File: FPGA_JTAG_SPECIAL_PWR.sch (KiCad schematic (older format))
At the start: 18 parts, among them U900 GW1N-9LQ100

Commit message: Stuff
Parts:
- added C36, C37, C38, C39, C56, C57, C58, C59, C60: 100nF_0603_Ceramic_Capacitor,_10%,_X7R,_25V, symbol OpenVent:100nF_0603_Ceramic_Capacitor,_10%,_X7R,_25V
- added C62, C63: 1uF_0603_Ceramic_Capacitor,_10%,_50V,_X5R, Capacitor_SMD:C_0603_1608Metric, symbol OpenVent:1uF_0603_Ceramic_Capacitor,_10%,_50V,_X5R
- added C65, C66: 10uF_0805_Ceramic_Capacitor_10%_X7R_10V, Capacitor_SMD:C_0805_2012Metric, symbol OpenVent:10uF_0805_Ceramic_Capacitor_10%_X7R_10V
- gave numbers to parts that had none: 13
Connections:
- wire segments 84 -> 139
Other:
- note added: "200 Ohm Res on the reset to GND"
- note added: "Fix arrow direction\n\n"
- note added: "HAS TO BE LDO"
- note added: "Same value caps. Occaisional big one."
- note added: "change to 0.1uF\n"

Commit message: First cut at a 3D rendering of the board.  Not too many missing models...
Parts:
- added R?: R_0603_200_0.1W_1%, Resistor_SMD:R_0603_1608Metric, symbol OpenVent:R_0603_200_0.1W_1%
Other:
- moved on the sheet: C24, C36, C37, C38, C39, C56, C57, C58, C59, C60, C62, C63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

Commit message: Changes some stuff
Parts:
- removed C24: 10uF_0805_Ceramic_Capacitor_10%_X7R_10V, Capacitor_SMD:C_0805_2012Metric, symbol OpenVent:10uF_0805_Ceramic_Capacitor_10%_X7R_10V
- removed C62, C63: 1uF_0603_Ceramic_Capacitor,_10%,_50V,_X5R, Capacitor_SMD:C_0603_1608Metric, symbol OpenVent:1uF_0603_Ceramic_Capacitor,_10%,_50V,_X5R
- added C21, C24, C61, C62: 100nF_0603_Ceramic_Capacitor,_10%,_X7R,_25V, symbol OpenVent:100nF_0603_Ceramic_Capacitor,_10%,_X7R,_25V
- added C63: 10uF_0805_Ceramic_Capacitor_10%_X7R_10V, Capacitor_SMD:C_0805_2012Metric, symbol OpenVent:10uF_0805_Ceramic_Capacitor_10%_X7R_10V
- gave numbers to parts that had none: 1
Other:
- note removed: "200 Ohm Res on the reset to GND"
- note removed: "Same value caps. Occaisional big one."
- note removed: "change to 0.1uF\n"
- moved on the sheet: C66

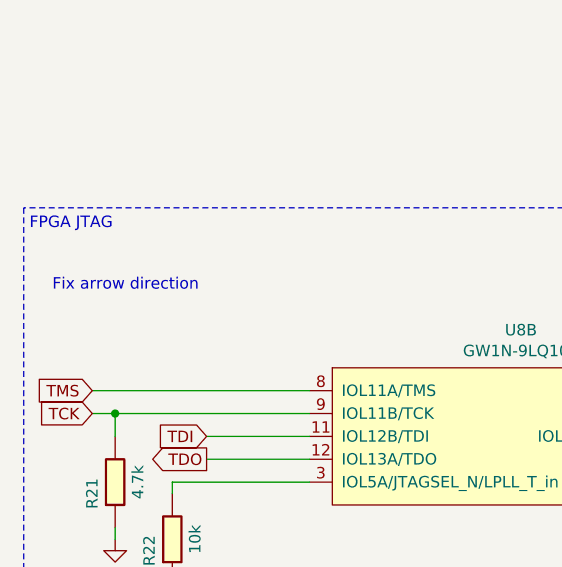
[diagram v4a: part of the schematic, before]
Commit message: Went through the whole circuit and made a note of what needs changing
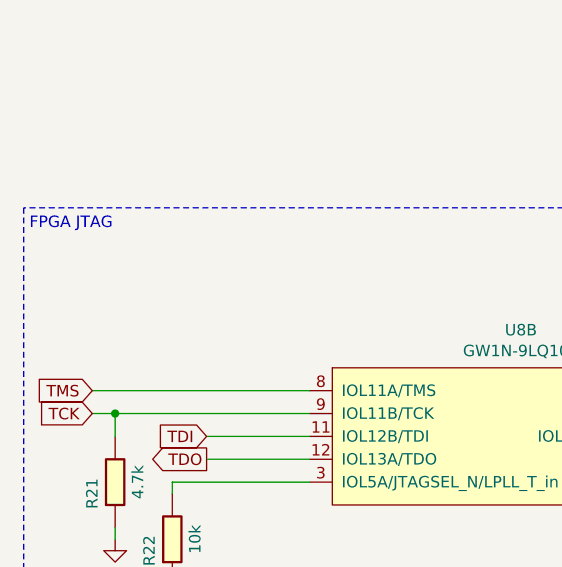
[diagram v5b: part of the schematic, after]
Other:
- note removed: "Fix arrow direction\n\n"
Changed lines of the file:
@@
 Text Notes 6875 1025 0    50   ~ 0
 HAS TO BE LDO
-Text Notes 1025 4850 0    50   ~ 0
-Fix arrow direction\n\n
 $Comp
 L OpenVent:12k_0603_Chip_Resistor,_1%,_0.1W R?

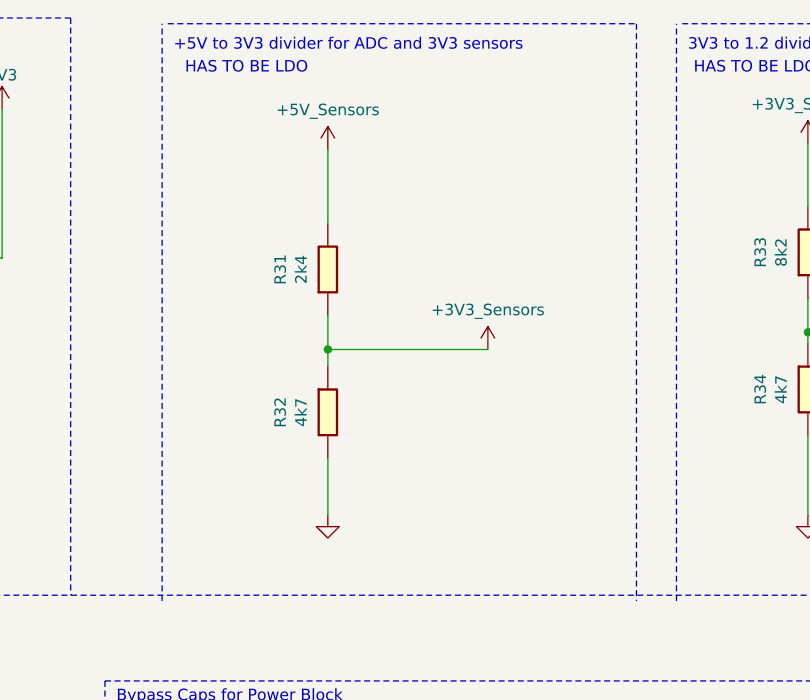
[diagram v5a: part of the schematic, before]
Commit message: Detailed description of changes below:
Sheet 2:
WD protection: 33ohm resistor in series in each line and then on the side between the resistor and micro put the ESD diode
ferrite beads and ESD prot on JP2
NRST PULLED UP TO 3V3Always on
VDD USB to 3V3
Sheet 6:
Oscillator out put to pin 40, got rud of 15pf
pin one pull up to 3v3 by 10k
Sheet 7:
changed 3V3 sensors from divider to LDO
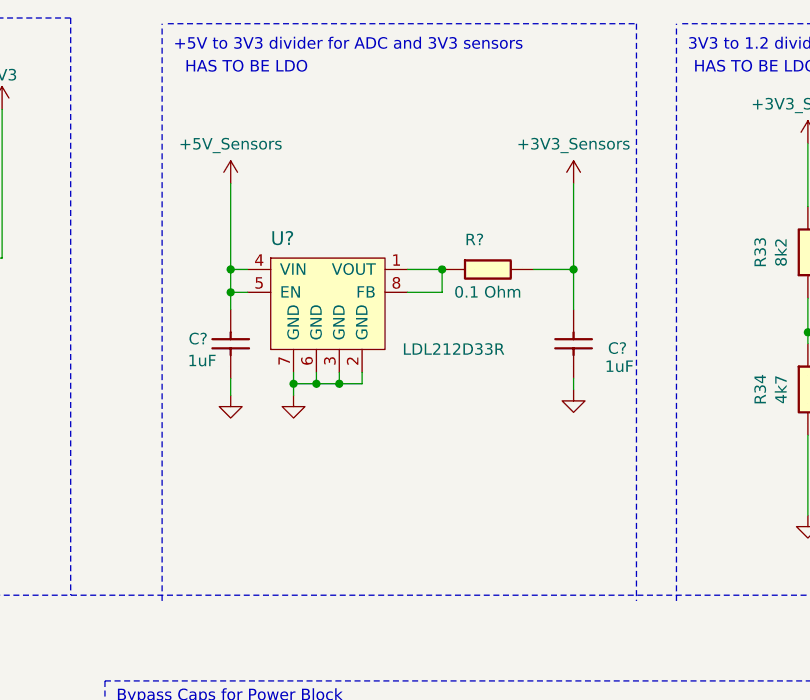
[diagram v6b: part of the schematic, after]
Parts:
- removed R31: 2k4_0603_Chip_Resistor,_1%,_0.1W, Resistor_SMD:R_0603_1608Metric, symbol OpenVent:2k4_0603_Chip_Resistor,_1%,_0.1W
- removed R32: 4k7_0603_Chip_Resistor,_1%,_0.1W, symbol OpenVent:4k7_0603_Chip_Resistor,_1%,_0.1W
- added C? (x2): 1uF_0603_Ceramic_Capacitor,_10%,_50V,_X5R, Capacitor_SMD:C_0603_1608Metric, symbol OpenVent:1uF_0603_Ceramic_Capacitor,_10%,_50V,_X5R
- added R?: 0R1_0603_Chip_Resistor,_1%,_0.1W, Resistor_SMD:R_0603_1608Metric, symbol OpenVent:0R1_0603_Chip_Resistor,_1%,_0.1W
- added U?: LDL212D33R, Package_SO:SO-8_5.3x6.2mm_P1.27mm, symbol OpenVent:LDL212D33R
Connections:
- net +3.3V: now also C?.1, R?.2
- net +5V: now also C?.2, U?.4 (VIN), U?.5 (EN)
- net GND: now also C?.1, C?.2, U?.2 (GND), U?.3 (GND), U?.6 (GND), U?.7 (GND)
- new net: R?.1, U?.1 (VOUT), U?.8 (FB)
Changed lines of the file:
@@
 	3625 1550 3625 1675
-$Comp
-L OpenVent:4k7_0603_Chip_Resistor,_1%,_0.1W R32
-U 1 1 5FCAA592
-P 7600 2400
-F 0 "R32" H 7500 2707 50  0000 C CNN
-F 1 "4k7_0603_Chip_Resistor,_1%,_0.1W" H 7600 2400 50  0001 C CNN
-F 2 "" H 7600 2400 50  0001 C CNN
-F 3 "" H 7600 2400 60  0001 C CNN
-F 4 "4k7" H 7500 2616 50  0000 C CNN "Val"
-F 5 "1%" H 7600 2400 50  0001 C CNN "Tolerance"
-F 6 "0.1W" H 7600 2400 50  0001 C CNN "Watt"
-	1    7600 2400
-	0    -1   -1   0
-$EndComp
-$Comp
-L OpenVent:2k4_0603_Chip_Resistor,_1%,_0.1W R31
-U 1 1 5FCB7193
-P 7400 1975
-F 0 "R31" H 7500 2082 50  0000 C CNN
-F 1 "2k4_0603_Chip_Resistor,_1%,_0.1W" H 7400 1975 50  0001 C CNN
-F 2 "Resistor_SMD:R_0603_1608Metric" H 7400 1975 50  0001 C CNN
-F 3 "" H 7400 1975 50  0001 C CNN
-F 4 "2k4" H 7500 1991 50  0000 C CNN "Val"
-F 5 "1%" H 7400 1975 50  0001 C CNN "Tolerance"
-F 6 "0.1W" H 7400 1975 50  0001 C CNN "Watt"
-	1    7400 1975
-	0    -1   -1   0
-$EndComp
 $Comp
 L OpenVent:8k2_0603_Chip_Resistor,_1%,_0.1W R33
@@
 	0    -1   -1   0
 $EndComp
-Wire Wire Line
-	7500 2300 7500 2225
 $Comp
 L OpenVent:GND #PWR?
 U 1 1 5FCCFD82
-P 7500 2950
+P 7075 2425
 AR Path="/5F8F8987/5FCCFD82" Ref="#PWR?"  Part="1"
 AR Path="/5FB692C4/5FCCFD82" Ref="#PWR064"  Part="1"
 AR Path="/5FBE8499/5FCCFD82" Ref="#PWR068"  Part="1"
-F 0 "#PWR068" H 7500 2700 50  0001 C CNN
-F 1 "GND" H 7500 2800 50  0001 C CNN
-F 2 "" H 7500 2950 50  0001 C CNN
-F 3 "" H 7500 2950 50  0001 C CNN
-	1    7500 2950
-	1    0    0    -1
-$EndComp
-Wire Wire Line
-	7500 2700 7500 2950
-Wire Wire Line
-	7500 2225 8200 2225
-Connection ~ 7500 2225
-Wire Wire Line
-	7500 2225 7500 2075
-Wire Wire Line
-	7500 1350 7500 1675
+F 0 "#PWR068" H 7075 2175 50  0001 C CNN
+F 1 "GND" H 7075 2275 50  0001 C CNN
+F 2 "" H 7075 2425 50  0001 C CNN
+F 3 "" H 7075 2425 50  0001 C CNN
+	1    7075 2425
+	1    0    0    -1
+$EndComp
 $Comp
 L OpenVent:GND #PWR?
@@
 L OpenVent:+5V_Sensors #PWR067
 U 1 1 5FBC8B4F
-P 7500 1350
-F 0 "#PWR067" H 7500 1200 50  0001 C CNN
-F 1 "+5V_Sensors" H 7500 1523 50  0000 C CNN
-F 2 "" H 7500 1350 50  0001 C CNN
-F 3 "" H 7500 1350 50  0001 C CNN
-	1    7500 1350
+P 7075 1500
+F 0 "#PWR067" H 7075 1350 50  0001 C CNN
+F 1 "+5V_Sensors" H 7075 1673 50  0000 C CNN
+F 2 "" H 7075 1500 50  0001 C CNN
+F 3 "" H 7075 1500 50  0001 C CNN
+	1    7075 1500
 	1    0    0    -1
 $EndComp
@@
 Text Notes 5475 1600 1    50   ~ 0
 DO NOT FIT
-Wire Wire Line
-	5175 1825 6075 1825
 Wire Wire Line
 	2325 1800 2325 2325
@@
 L OpenVent:+3V3_Sensors #PWR?
 U 1 1 5FC9D143
-P 8200 2225
+P 8575 1500
 AR Path="/5FC9D143" Ref="#PWR?"  Part="1"
 AR Path="/5FB692C4/5FC9D143" Ref="#PWR?"  Part="1"
 AR Path="/5FBE8499/5FC9D143" Ref="#PWR069"  Part="1"
-F 0 "#PWR069" H 8200 2075 50  0001 C CNN
-F 1 "+3V3_Sensors" H 8200 2398 50  0000 C CNN
-F 2 "" H 8200 2225 50  0001 C CNN
-F 3 "" H 8200 2225 50  0001 C CNN
-	1    8200 2225
+F 0 "#PWR069" H 8575 1350 50  0001 C CNN
+F 1 "+3V3_Sensors" H 8575 1673 50  0000 C CNN
+F 2 "" H 8575 1500 50  0001 C CNN
+F 3 "" H 8575 1500 50  0001 C CNN
+	1    8575 1500
 	1    0    0    -1
 $EndComp
@@
 Wire Wire Line
 	9525 5325 10150 5325
+$Comp
+L OpenVent:GND #PWR?
+U 1 1 5FEC0980
+P 7350 2425
+AR Path="/5F99D63D/5FEC0980" Ref="#PWR?"  Part="1"
+AR Path="/5FBE8499/5FEC0980" Ref="#PWR?"  Part="1"
+F 0 "#PWR?" H 7350 2425 50  0001 C CNN
+F 1 "GND" H 7350 2425 50  0001 C CNN
+F 2 "" H 7350 2425 50  0001 C CNN
+F 3 "" H 7350 2425 50  0001 C CNN
+	1    7350 2425
+	1    0    0    -1
+$EndComp
+$Comp
+L OpenVent:LDL212D33R U?
+U 1 1 5FEC0997
+P 7500 2025
+AR Path="/5F99D63D/5FEC0997" Ref="U?"  Part="1"
+AR Path="/5FBE8499/5FEC0997" Ref="U?"  Part="1"
+F 0 "U?" H 7250 2275 60  0000 L BNN
+F 1 "LDL212D33R" H 8050 1825 50  0000 C CNN
+F 2 "Package_SO:SO-8_5.3x6.2mm_P1.27mm" H 7500 2025 50  0001 C CNN
+F 3 "https://www.st.com/resource/en/datasheet/ldl212.pdf" H 7500 2025 50  0001 C CNN
+F 4 "LDL212D33R" H 7500 2025 50  0001 C CNN "Mfr_PN"
+F 5 "STMicroelectronics" H 7500 2025 50  0001 C CNN "Mfr"
+F 6 "1.2A" H 7500 2025 50  0001 C CNN "Current"
+F 7 "LDOVOLTAGE REGULATORS 1.2A LOW D" H 7500 2025 50  0001 C CNN "Desc"
+F 8 "Linear Voltage Regulator IC Output 1.2A 8-SO" H 7500 2025 50  0001 C CNN "Detailed"
+F 9 "DigiKey" H 7500 2025 50  0001 C CNN "DistName"
+F 10 "497-18287-2-ND" H 7500 2025 50  0001 C CNN "Dist_PN"
+	1    7500 2025
+	1    0    0    -1
+$EndComp
+$Comp
+L OpenVent:1uF_0603_Ceramic_Capacitor,_10%,_50V,_X5R C?
+U 1 1 5FEC09A0
+P 8675 2150
+AR Path="/5F99D63D/5FEC09A0" Ref="C?"  Part="1"
+AR Path="/5FBE8499/5FEC09A0" Ref="C?"  Part="1"
+F 0 "C?" V 8775 2200 50  0000 L BNN
+F 1 "1uF_0603_Ceramic_Capacitor,_10%,_50V,_X5R" V 8585 1960 50  0001 C CNN
+F 2 "Capacitor_SMD:C_0603_1608Metric" H 8585 1960 50  0001 C CNN
+F 3 "" H 8585 1960 50  0001 C CNN
+F 4 "10%" H 8675 2150 50  0001 C CNN "Tolerance"
+F 5 "1uF" V 8825 2250 50  0000 C CNN "Val"
+F 6 "50V" H 8675 2150 50  0001 C CNN "Voltage"
+	1    8675 2150
+	0    1    1    0
+$EndComp
+$Comp
+L OpenVent:0R1_0603_Chip_Resistor,_1%,_0.1W R?
+U 1 1 5FEC09A9
+P 8100 1775
+AR Path="/5FEC09A9" Ref="R?"  Part="1"
+AR Path="/5F99D63D/5FEC09A9" Ref="R?"  Part="1"
+AR Path="/5FBE8499/5FEC09A9" Ref="R?"  Part="1"
+F 0 "R?" H 8100 1775 50  0000 L BNN
+F 1 "0R1_0603_Chip_Resistor,_1%,_0.1W" H 8100 1525 50  0001 C CNN
+F 2 "Resistor_SMD:R_0603_1608Metric" H 8100 1435 50  0001 C CNN
+F 3 "" H 8100 1435 50  0001 C CNN
+F 4 "1%" V -300 -4525 50  0001 C CNN "Tolerance"
+F 5 "0.1 Ohm" H 8200 1575 50  0000 C CNN "Val"
+F 6 "0.1W" H 8100 1775 50  0001 C CNN "Watt"
+	1    8100 1775
+	1    0    0    -1
+$EndComp
+$Comp
+L OpenVent:1uF_0603_Ceramic_Capacitor,_10%,_50V,_X5R C?
+U 1 1 5FEC09B2
+P 6975 2250
+AR Path="/5F99D63D/5FEC09B2" Ref="C?"  Part="1"
+AR Path="/5FBE8499/5FEC09B2" Ref="C?"  Part="1"
+F 0 "C?" V 7075 2250 50  0000 L BNN
+F 1 "1uF_0603_Ceramic_Capacitor,_10%,_50V,_X5R" V 6885 2060 50  0001 C CNN
+F 2 "Capacitor_SMD:C_0603_1608Metric" H 6885 2060 50  0001 C CNN
+F 3 "" H 6885 2060 50  0001 C CNN
+F 4 "10%" H 6975 2250 50  0001 C CNN "Tolerance"
+F 5 "1uF" V 6950 2275 50  0000 C CNN "Val"
+F 6 "50V" H 6975 2250 50  0001 C CNN "Voltage"
+	1    6975 2250
+	0    -1   -1   0
+$EndComp
+Wire Wire Line
+	7850 1875 8000 1875
+Wire Wire Line
+	7850 1975 8000 1975
+Wire Wire Line
+	8000 1975 8000 1875
+Wire Wire Line
+	7350 2325 7350 2375
+Wire Wire Line
+	7350 2375 7450 2375
+Wire Wire Line
+	7650 2375 7650 2325
+Connection ~ 7350 2375
+Wire Wire Line
+	7350 2375 7350 2425
+Wire Wire Line
+	7550 2325 7550 2375
+Connection ~ 7550 2375
+Wire Wire Line
+	7550 2375 7650 2375
+Wire Wire Line
+	7450 2325 7450 2375
+Connection ~ 7450 2375
+Wire Wire Line
+	7450 2375 7550 2375
+Wire Wire Line
+	5175 1825 6075 1825
+Wire Wire Line
+	7075 1500 7075 1875
+Connection ~ 7075 1875
+Wire Wire Line
+	7075 1875 7150 1875
+Wire Wire Line
+	7075 1875 7075 1975
+Wire Wire Line
+	7075 1975 7150 1975
+Wire Wire Line
+	7075 2425 7075 2350
+Wire Wire Line
+	7075 2050 7075 1975
+Connection ~ 7075 1975
+Connection ~ 8000 1875
+Wire Wire Line
+	8575 1500 8575 1875
+Wire Wire Line
+	8400 1875 8575 1875
+Connection ~ 8575 1875
+Wire Wire Line
+	8575 1875 8575 2050
+$Comp
+L OpenVent:GND #PWR?
+U 1 1 5FF69BE4
+P 8575 2400
+AR Path="/5F99D63D/5FF69BE4" Ref="#PWR?"  Part="1"
+AR Path="/5FBE8499/5FF69BE4" Ref="#PWR?"  Part="1"
+F 0 "#PWR?" H 8575 2400 50  0001 C CNN
+F 1 "GND" H 8575 2400 50  0001 C CNN
+F 2 "" H 8575 2400 50  0001 C CNN
+F 3 "" H 8575 2400 50  0001 C CNN
+	1    8575 2400
+	1    0    0    -1
+$EndComp
+Wire Wire Line
+	8575 2400 8575 2350
 $EndSCHEMATC
